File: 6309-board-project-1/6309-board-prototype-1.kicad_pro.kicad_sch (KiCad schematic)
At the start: 17 parts, among them J1 PWR, J2 FTDI, SW1 Reset, U1 HD63C09, U2 62256, U3 28C256, U4 16C550, U5 74LS04, X1 12MHz, X2 1.8432MHz

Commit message: almost done with schematic
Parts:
- removed SW1: Reset, symbol Switch:SW_Push_SPDT
- added C10: 100nF, symbol Device:C_Small
- added C8: 0.01uf, symbol Device:C_Small
- added C9: 0.01uF, symbol Device:C_Small
- added R1: 1K, symbol Device:R_Small_US
- added SW1: SW_Push, symbol Switch:SW_Push
- added U6: 4068, symbol 4xxx_IEEE:4068
- added U8: 74HCT32, symbol 74xx:74LS32
- C1, C2, C3, C6, C7: value 0.01uf -> 0.01uF
- J1: footprint (none) -> Connector_PinHeader_2.54mm:PinHeader_1x02_P2.54mm_Vertical
- J2: footprint (none) -> Connector_PinHeader_2.54mm:PinHeader_1x06_P2.54mm_Vertical
- U5: value 74LS04 -> 74HCT04; symbol 74xx:74LS04 -> 74xx:74HCT04
- X1: footprint (none) -> Crystal:Crystal_HC49-U_Vertical
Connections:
- net A8 is gone; now on net A15: U1.16 (A8), U2.25 (A8), U3.25 (A8)
- net +5V: now also C8.1, R1.2, U6.14 (Vdd)
- net A10: now also U6.4 (C)
- net A11: now also U6.5 (D)
- net A12: now also U6.9 (E)
- net A13: now also U6.10 (F)
- net A14: now also U6.11 (G)
- net A15: now also U5.5, U6.2 (A), U8.1, U8.2
- net A9: now also U6.3 (B)
- net GND: now also C10.1, C8.2, C9.2, SW1.2, U6.7 (Vss), U8.7 (GND)
- net at U5.8: now also U5.9
- net at U2.20 (~{CS}): now also U2.22 (~{OE}), U8.3
- net at U4.12 (CS0): now also U6.1 (K)
- net !A15: now reaches U5.6
- net !A15: now also U3.20 (~{CS}), U3.22 (~{OE}), U6.12 (H)
- new net: C10.2, R1.1, SW1.1
- new net: C9.1, U8.14 (VCC)
- no-connect marks 11 -> 12
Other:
- note added: "GLUE LOGIC"
- note added: "POWER + RESET SWITCH"
- note removed: "MANUAL RESET SWITCH"
- moved on the sheet: C7, U5C, U5G

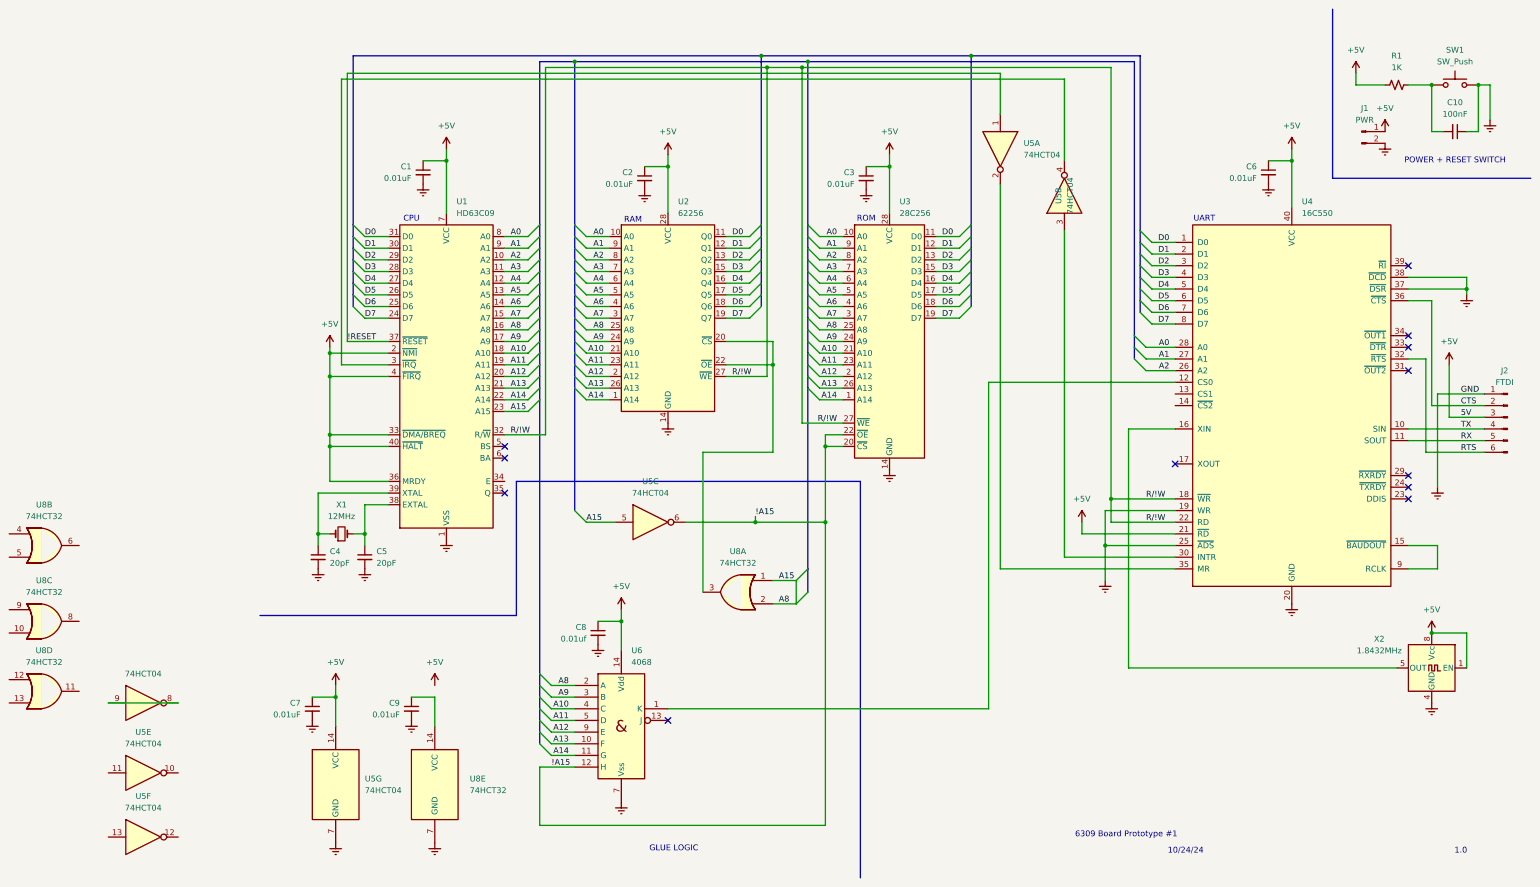
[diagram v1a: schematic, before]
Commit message: add footprints to schematic
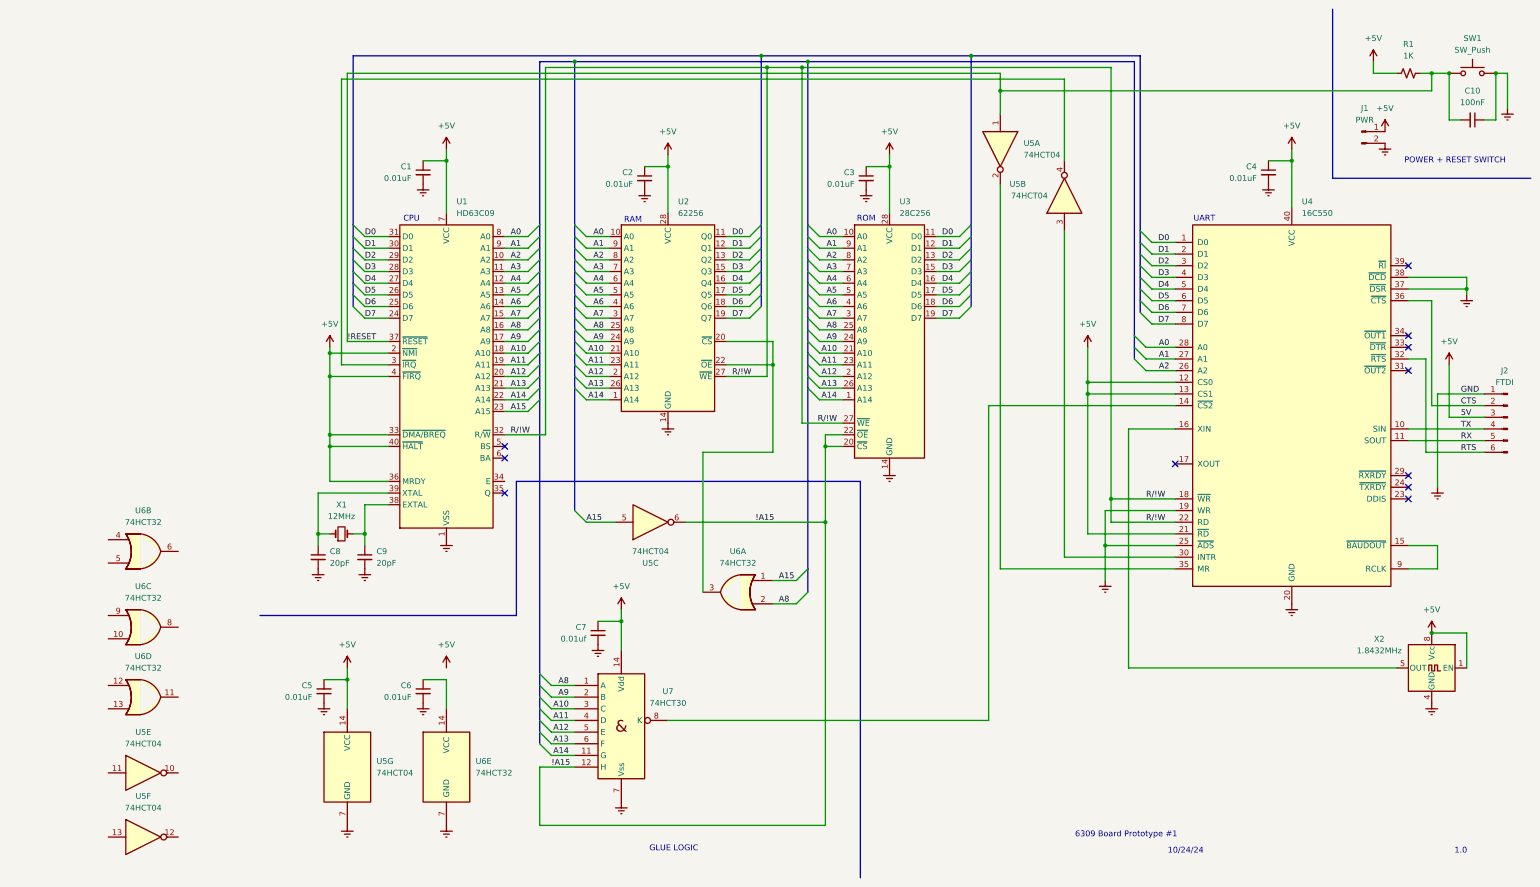
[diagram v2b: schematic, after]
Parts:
- removed unit 4 of U5
- C1, C2, C3: footprint (none) -> Capacitor_THT:C_Disc_D5.0mm_W2.5mm_P2.50mm
- C10: footprint (none) -> Capacitor_THT:C_Disc_D5.0mm_W2.5mm_P5.00mm
- C4: renamed from C6; footprint (none) -> Capacitor_THT:C_Disc_D5.0mm_W2.5mm_P2.50mm
- C5: renamed from C7; footprint (none) -> Capacitor_THT:C_Disc_D5.0mm_W2.5mm_P2.50mm
- C6: renamed from C9; footprint (none) -> Capacitor_THT:C_Disc_D5.0mm_W2.5mm_P2.50mm
- C7: renamed from C8; footprint (none) -> Capacitor_THT:C_Disc_D5.0mm_W2.5mm_P2.50mm
- C8: renamed from C4; footprint (none) -> Capacitor_THT:C_Disc_D5.0mm_W2.5mm_P5.00mm
- C9: renamed from C5; footprint (none) -> Capacitor_THT:C_Disc_D5.0mm_W2.5mm_P5.00mm
- R1: footprint (none) -> Resistor_THT:R_Axial_DIN0207_L6.3mm_D2.5mm_P5.08mm_Vertical
- SW1: footprint (none) -> Button_Switch_THT:SW_PUSH_6mm_H5mm
- U1, U4: footprint Package_DIP:DIP-40_W15.24mm -> Package_DIP:DIP-40_W15.24mm_Socket
- U2: footprint Package_DIP:DIP-28_W15.24mm -> Package_DIP:DIP-28_W15.24mm_Socket
- U3: footprint (none) -> Package_DIP:DIP-28_W7.62mm_Socket
- U5: footprint (none) -> Package_DIP:DIP-14_W7.62mm_Socket
- U6: renamed from U8; footprint (none) -> Package_DIP:DIP-14_W7.62mm_Socket
- U7: renamed from U6; value 4068 -> 74HCT30; footprint (none) -> Package_DIP:DIP-14_W7.62mm_Socket
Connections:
- net !RESET: now also C10.2, R1.1, SW1.1
- net +5V: now also U4.12 (CS0), U4.13 (CS1)
- net A10: now also U7.3 (C); no longer U7.4 (C)
- net A11: now also U7.4 (D); no longer U7.5 (D)
- net A12: now also U7.5 (E); no longer U7.9 (E)
- net A13: now also U7.6 (F); no longer U7.10 (F)
- net A15: no longer U1.16 (A8), U2.25 (A8), U3.25 (A8), U6.2, U7.2 (A)
- net A9: now also U7.2 (B); no longer U7.3 (B)
- net A8: now reaches U7.1 (A)
- net A8: now also U1.16 (A8), U2.25 (A8), U3.25 (A8), U6.2; no longer U4.12 (CS0)
- net at U7.8 (K): now also U4.14 (~{CS2})
- no-connect marks 12 -> 11
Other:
- moved on the sheet: C10, C5, C6, R1, SW1, U5G, U6B, U6C, U6D, U6E

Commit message: changed rom, added correct switch, added a million footprints
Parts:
- removed C10: 100nF, Capacitor_THT:C_Disc_D5.0mm_W2.5mm_P5.00mm, symbol Device:C_Small
- removed R1: 1K, Resistor_THT:R_Axial_DIN0207_L6.3mm_D2.5mm_P5.08mm_Vertical, symbol Device:R_Small_US
- removed SW1: SW_Push, Button_Switch_THT:SW_PUSH_6mm_H5mm, symbol Switch:SW_Push
- removed X2: 1.8432MHz, Oscillator:Oscillator_DIP-8, symbol Oscillator:CXO_DIP8
- added C11: 47pF, Capacitor_THT:C_Disc_D5.0mm_W2.5mm_P5.00mm, symbol Device:C_Small
- added C12: 18pF, Custom:CAP_C317_KEM, symbol Custom:C317C180J5G5TA
- added C13: 1uF, Custom:CAP_C330C_MR_X7R_KEM, symbol Custom:C330C105J5R5TA
- added C14, C16: 0.1uF, Custom:CAP_C320C_MR_X7R_KEM, symbol Custom:C320C104J5R5TA7301
- added C15: 0.01uF, Custom:CAP_C315C_MR_X7R_KEM, symbol Custom:C315C103J5R5TA
- added R2: 1.5k, Resistor_THT:R_Axial_DIN0207_L6.3mm_D2.5mm_P5.08mm_Vertical, symbol Device:R_Small_US
- added R3: 1M, Resistor_THT:R_Axial_DIN0207_L6.3mm_D2.5mm_P5.08mm_Vertical, symbol Device:R_Small_US
- added R4, R5, R6, R7, R8, R9: 100K, Resistor_THT:R_Axial_DIN0207_L6.3mm_D2.5mm_P5.08mm_Vertical, symbol Device:R_Small_US
- added SW1: B3F-1000, SW_B3F-1000_OMR, symbol SW_B3F-1000_OMR:B3F-1000
- added X2: 1.8432 MHz, Crystal:Crystal_HC49-U_Vertical, symbol Device:Crystal_Small
- C1, C2, C3, C4, C5, C6: value 0.01uF -> 0.1uF; footprint Capacitor_THT:C_Disc_D5.0mm_W2.5mm_P2.50mm -> Custom:CAP_C320C_MR_X7R_KEM; symbol Device:C_Small -> Custom:C320C104J5R5TA7301
- C7: value 0.01uf -> 0.1uF; footprint Capacitor_THT:C_Disc_D5.0mm_W2.5mm_P2.50mm -> Custom:CAP_C320C_MR_X7R_KEM; symbol Device:C_Small -> Custom:C320C104J5R5TA7301
- C8, C9: value 20pF -> 24pF; footprint Capacitor_THT:C_Disc_D5.0mm_W2.5mm_P5.00mm -> Custom:CAP_C317_KEM; symbol Device:C_Small -> Custom:C317C240J5G5TA
- U1: value HD63C09 -> 63C09; symbol CPU_NXP_6800:MC6809 -> Custom:HD63C09
- U2: symbol Memory_RAM:KM62256CLP -> Custom:AS6C62256-55PCN
- U3: value 28C256 -> 39FS010; footprint Package_DIP:DIP-28_W7.62mm_Socket -> Package_DIP:DIP-32_W15.24mm; symbol Memory_EEPROM:28C256 -> Custom:SST39SF010A
- U4: symbol Interface_UART:16550 -> Custom:TL16C550
- U6: symbol 74xx:74LS32 -> Custom:74HCT32
- U7: symbol 4xxx_IEEE:4068 -> Custom:74HCT30
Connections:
- net !A15: now also U3.24 (~{OE}); no longer U3.20 (~{CS})
- net !RESET: now also U1.3 (~{IRQ}), U5.4, C16.2, R9.1
- net +5V: now also C6.1, U3.32 (VDD), U6.14 (VCC), C13.1, C14.1, C15.1, R5.2, R6.2, R9.2, SW1.1; no longer U1.2 (~{NMI}), U1.33 (~{DMA/BREQ}), U1.36 (MRDY), U1.4 (~{FIRQ}), U1.40 (~{HALT}), U3.28 (VCC), U4.12 (CS0), U4.13 (CS1), U4.21 (~{RD})
- net A0: now also U3.12 (A0); no longer U3.10 (A0)
- net A1: now also U3.11 (A1); no longer U3.9 (A1)
- net A10: now also U3.23 (A10); no longer U3.21 (A10)
- net A11: now also U3.25 (A11); no longer U3.23 (A11)
- net A12: now also U3.4 (A12); no longer U3.2 (A12)
- net A13: now also U3.28 (A13); no longer U3.26 (A13)
- net A14: now also U3.29 (A14); no longer U3.1 (A14)
- net A2: now also U3.10 (A2); no longer U3.8 (A2)
- net A3: now also U3.9 (A3); no longer U3.7 (A3)
- net A4: now also U3.8 (A4); no longer U3.6 (A4)
- net A5: now also U3.7 (A5); no longer U3.5 (A5)
- net A6: now also U3.6 (A6); no longer U3.4 (A6)
- net A7: now also U3.5 (A7); no longer U3.3 (A7)
- net A8: now also U3.27 (A8); no longer U3.25 (A8)
- net A9: now also U3.26 (A9); no longer U3.24 (A9)
- net D0: now also U3.13 (DQ0); no longer U3.11 (D0)
- net D1: now also U3.14 (DQ1); no longer U3.12 (D1)
- net D2: now also U3.15 (DQ2); no longer U3.13 (D2)
- net D3: now also U3.17 (DQ3); no longer U3.15 (D3)
- net D4: now also U3.18 (DQ4); no longer U3.16 (D4)
- net D5: now also U3.19 (DQ5); no longer U3.17 (D5)
- net D6: now also U3.20 (DQ6); no longer U3.18 (D6)
- net D7: now also U3.21 (DQ7); no longer U3.19 (D7)
- net GND: now also U3.16 (VSS), C11.2, C12.2, C13.2, C14.2, C15.2, C16.1, R4.1, R7.1, R8.1, SW1.4; no longer U3.14 (GND), U4.19 (WR), U4.25 (~{ADS}), U4.37 (~{DSR}), U4.38 (~{DCD})
- net R/!W: now also U3.31 (~{WE}); no longer U3.27 (~{WE})
- net at U4.16 (XIN): now also C12.1, R3.1, X2.1
- net at U4.17 (XOUT): now also R2.2
- new net: C11.1, R2.1, R3.2, X2.2
- new net: R8.2, U3.2 (A16), U3.3 (A15)
- new net: R7.2, U4.19 (WR), U4.25 (~{ADS})
- new net: R5.1, U4.12 (CS0), U4.13 (CS1), U4.21 (~{RD})
- new net: R4.2, U4.37 (~{DSR}), U4.38 (~{DCD})
- new net: R6.1, U1.2 (~{NMI}), U1.33 (~{DMA/BREQ}), U1.36 (MRDY), U1.4 (~{FIRQ}), U1.40 (~{HALT})
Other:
- note added: "POWER"
- note added: "RESET SWITCH"
- note removed: "POWER + RESET SWITCH"
- moved on the sheet: C3, J1, U6A

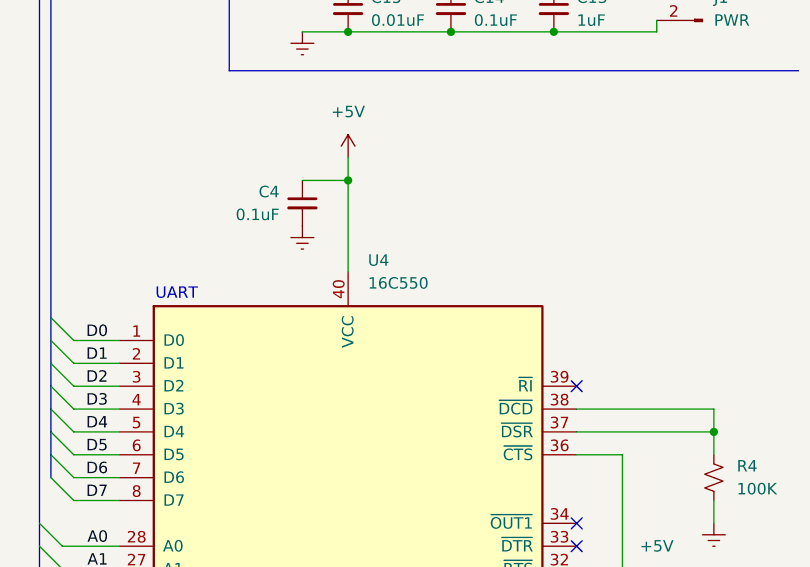
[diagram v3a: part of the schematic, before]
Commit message: switch from Tl16C550 to PC16550D due to availability
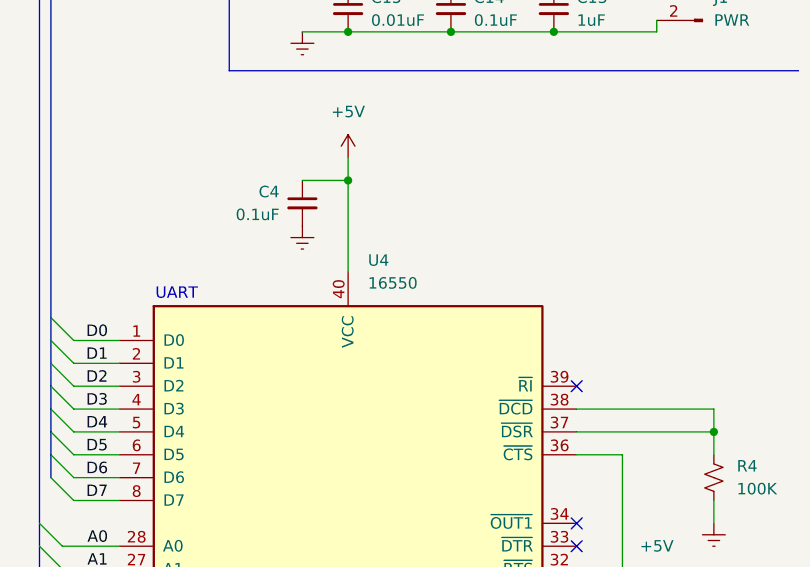
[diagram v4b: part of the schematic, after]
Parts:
- U4: value 16C550 -> 16550
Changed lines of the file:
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@@
 			)
 		)
-		(property "Value" "16C550"
+		(property "Value" "16550"
 			(at 237.1441 54.61 0)
 			(effects
@@
 			)
 		)
-		(property "Datasheet" "https://www.ti.com/lit/ds/symlink/tl16c550c.pdf"
+		(property "Datasheet" "https://media.digikey.com/pdf/Data%20Sheets/Texas%20Instruments%20PDFs/PC16550D.pdf"
 			(at 234.95 96.52 0)
 			(effects
@@
 			)
 		)
-		(property "Description" "TL16C550, Universal Asynchronous Receiver/Transmitter with FIFOs, PDIP-40"
+		(property "Description" "PC16550D Universal Asynchronous Receiver/Transmitter With FIFOs"
 			(at 234.95 96.52 0)
 			(effects

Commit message: fixed schematic, started pcb
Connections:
- net !RESET: no longer U1.3 (~{IRQ}), U5.4
- new net: U1.3 (~{IRQ}), U5.4
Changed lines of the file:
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@@
 	)
 	(junction
-		(at 165.1 25.4)
-		(diameter 0)
-		(color 0 0 0 0)
-	)
-	(junction
 		(at 157.48 182.88)
 		(diameter 0)
@@
 	(wire
 		(pts
-			(xy 165.1 25.4) (xy 165.1 24.13)
+			(xy 165.1 24.13) (xy 165.1 162.56)
 		)
 		(stroke
@@
 	(wire
 		(pts
-			(xy 165.1 25.4) (xy 185.42 25.4)
+			(xy 27.94 25.4) (xy 185.42 25.4)
 		)
 		(stroke
@@
 		)
 	)
-	(wire
-		(pts
-			(xy 165.1 25.4) (xy 165.1 162.56)
-		)
-		(stroke
-			(width 0)
-			(type default)
-		)
-	)
 	(bus
 		(pts
@@
 		)
 		(stroke
-			(width 0)
-			(type default)
-		)
-	)
-	(wire
-		(pts
-			(xy 27.94 25.4) (xy 165.1 25.4)
-		)
-		(stroke

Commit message: schematic work
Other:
- moved on the sheet: R2, X2
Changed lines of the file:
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@@
 	)
 	(junction
-		(at 242.57 153.67)
-		(diameter 0)
-		(color 0 0 0 0)
-	)
-	(junction
 		(at 195.58 116.84)
 		(diameter 0)
@@
 	)
 	(junction
-		(at 257.81 26.67)
+		(at 240.03 146.05)
 		(diameter 0)
 		(color 0 0 0 0)
 	)
 	(junction
-		(at 242.57 146.05)
+		(at 257.81 26.67)
 		(diameter 0)
 		(color 0 0 0 0)
@@
 	)
 	(junction
+		(at 240.03 153.67)
+		(diameter 0)
+		(color 0 0 0 0)
+	)
+	(junction
 		(at 22.86 124.46)
 		(diameter 0)
@@
 	(wire
 		(pts
-			(xy 238.76 153.67) (xy 242.57 153.67)
+			(xy 223.52 153.67) (xy 240.03 153.67)
 		)
 		(stroke
@@
 	(wire
 		(pts
-			(xy 242.57 146.05) (xy 242.57 147.32)
+			(xy 240.03 146.05) (xy 240.03 147.32)
 		)
 		(stroke
@@
 	(wire
 		(pts
+			(xy 240.03 153.67) (xy 248.92 153.67)
+		)
+		(stroke
+			(width 0)
+			(type default)
+		)
+	)
+	(wire
+		(pts
 			(xy 185.42 129.54) (xy 209.55 129.54)
 		)
@@
 	(wire
 		(pts
-			(xy 242.57 152.4) (xy 242.57 153.67)
+			(xy 240.03 152.4) (xy 240.03 153.67)
 		)
 		(stroke
@@
 	(wire
 		(pts
-			(xy 196.85 146.05) (xy 242.57 146.05)
+			(xy 196.85 146.05) (xy 240.03 146.05)
 		)
 		(stroke
@@
 	(wire
 		(pts
-			(xy 242.57 146.05) (xy 248.92 146.05)
-		)
-		(stroke
-			(width 0)
-			(type default)
-		)
-	)
-	(wire
-		(pts
 			(xy 73.66 165.1) (xy 78.74 165.1)
 		)
@@
 		)
 	)
-	(wire
-		(pts
-			(xy 242.57 153.67) (xy 248.92 153.67)
-		)
-		(stroke
-			(width 0)
-			(type default)
-		)
-	)
 	(bus
 		(pts
@@
 	(wire
 		(pts
-			(xy 198.12 153.67) (xy 233.68 153.67)
+			(xy 198.12 153.67) (xy 218.44 153.67)
 		)
 		(stroke
@@
 	(wire
 		(pts
+			(xy 240.03 146.05) (xy 248.92 146.05)
+		)
+		(stroke
+			(width 0)
+			(type default)
+		)
+	)
+	(wire
+		(pts
 			(xy 160.02 77.47) (xy 154.94 77.47)
 		)
@@
 	(symbol
 		(lib_id "Device:Crystal_Small")
-		(at 242.57 149.86 90)
+		(at 240.03 149.86 90)
 		(mirror x)
 		(unit 1)
@@
 		(dnp no)
 		(property "Reference" "X2"
-			(at 240.03 148.5899 90)
+			(at 237.49 148.5899 90)
 			(effects
 				(font
@@
 		)
 		(property "Value" "1.8432 MHz"
-			(at 240.03 151.1299 90)
+			(at 237.49 151.1299 90)
 			(effects
 				(font
@@
 		)
 		(property "Footprint" "Crystal:Crystal_HC49-U_Vertical"
-			(at 242.57 149.86 0)
+			(at 240.03 149.86 0)
 			(effects
 				(font
@@
 		)
 		(property "Datasheet" "~"
-			(at 242.57 149.86 0)
+			(at 240.03 149.86 0)
 			(effects
 				(font
@@
 		)
 		(property "Description" "Two pin crystal, small symbol"
-			(at 242.57 149.86 0)
+			(at 240.03 149.86 0)
 			(effects
 				(font
@@
 		(lib_id "Device:R_Small_US")
 		(at 248.92 149.86 0)
+		(mirror y)
 		(unit 1)
 		(exclude_from_sim no)
@@
 		(dnp no)
 		(property "Reference" "R3"
-			(at 251.46 148.59 0)
+			(at 246.38 148.59 0)
 			(effects
 				(font
@@
 		)
 		(property "Value" "1M"
-			(at 251.46 151.13 0)
+			(at 246.38 151.13 0)
 			(effects
 				(font
@@
 	(symbol
 		(lib_id "Device:R_Small_US")
-		(at 236.22 153.67 270)
+		(at 220.98 153.67 270)
 		(unit 1)
 		(exclude_from_sim no)
@@
 		(dnp no)
 		(property "Reference" "R2"
-			(at 237.49 156.21 0)
+			(at 222.25 156.21 0)
 			(effects
 				(font
@@
 		)
 		(property "Value" "1.5k"
-			(at 234.95 156.21 0)
+			(at 219.71 156.21 0)
 			(effects
 				(font
@@
 		)
 		(property "Footprint" "Resistor_THT:R_Axial_DIN0207_L6.3mm_D2.5mm_P5.08mm_Vertical"
-			(at 236.22 153.67 0)
+			(at 220.98 153.67 0)
 			(effects
 				(font
@@
 		)
 		(property "Datasheet" "~"
-			(at 236.22 153.67 0)
+			(at 220.98 153.67 0)
 			(effects
 				(font
@@
 		)
 		(property "Description" "Resistor, small US symbol"
-			(at 236.22 153.67 0)
+			(at 220.98 153.67 0)
 			(effects
 				(font
